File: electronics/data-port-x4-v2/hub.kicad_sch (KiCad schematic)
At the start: 56 parts, among them J1 LEAD, Q1 2N7002, Q2 2N7002, Q3 2N7002, U1 USB2517I-JZX, U2 TCA6408ARGTR, U3 AP2114H-3.3TRG1, U4 H5VU25UC, U5 MAX809S, U6 TCA6408ARGTR, Y1 X322524MSB4SI

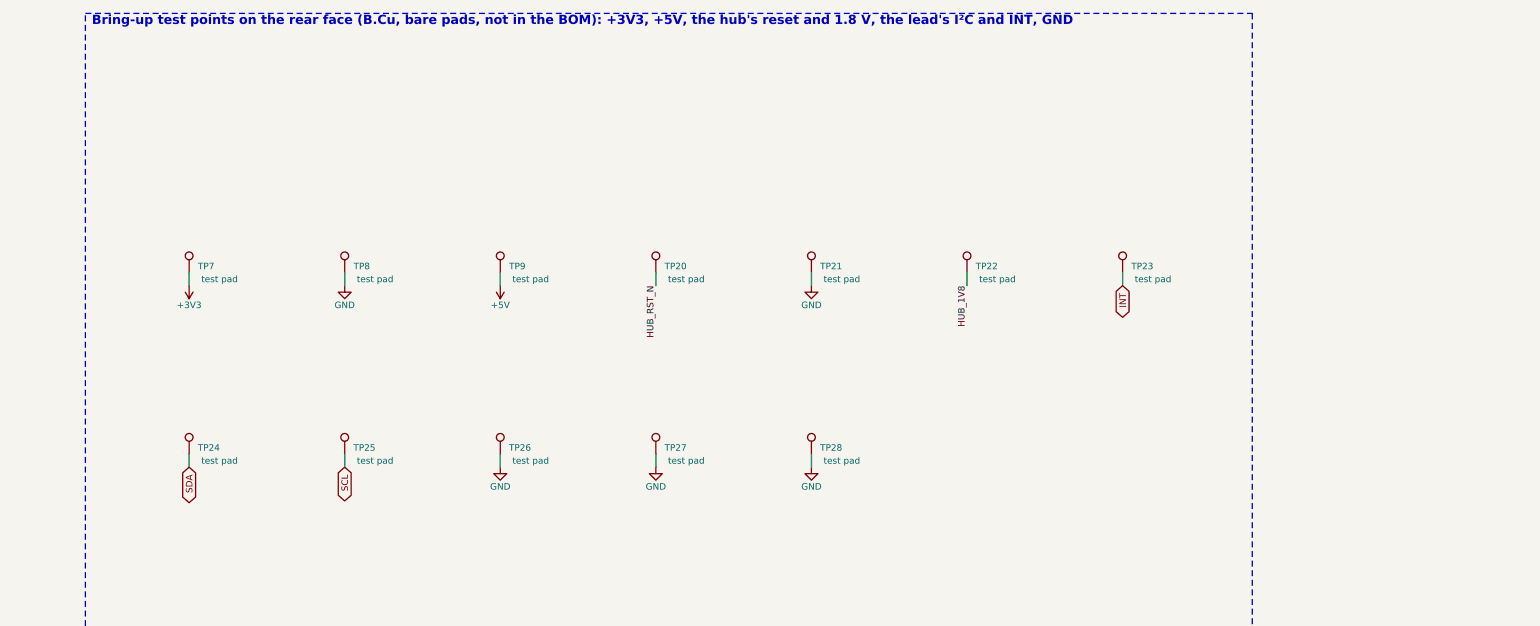
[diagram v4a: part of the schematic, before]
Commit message: DATA x4 v2: rear test pads on buses A-H and the expanders' RESET
Eve's DFT review asked for probe points on the eight crosspoint buses
and on both TCA6408A RESET lines, with a GND beside them.  Eleven bare
rear pads (TPS, out of the BOM and CPL, named on B.SilkS):

- TP29-TP36, buses A to H (1.0 mm), behind the co-processor's east
  side where all eight pass.  A, B, E and F sit on a rear track of their
  own, C, D and G beside one; H, front only, comes down a drawn via.
  Each goes where its bus passes, 2.6 mm or more from the next.
- TP37 GND (1.5 mm), with a drawn via east of it: the automatic one
  went west and moved RN8's +3V3 dog-bones.
- TP38 / TP39 EXP1 / EXP2 RST, each by its pull-up's via.

Every pad is 3.4 mm or more from a THT pad or J1.  The bus group
carries a LOGIC ONLY mark.  The router re-ran only for the new links:
BUS_H's front track moved 0.2 mm onto the new via, and two GND
dog-bones beside it turned.

Co-Authored-By: Claude Opus 5.5 <noreply@anthropic.com>
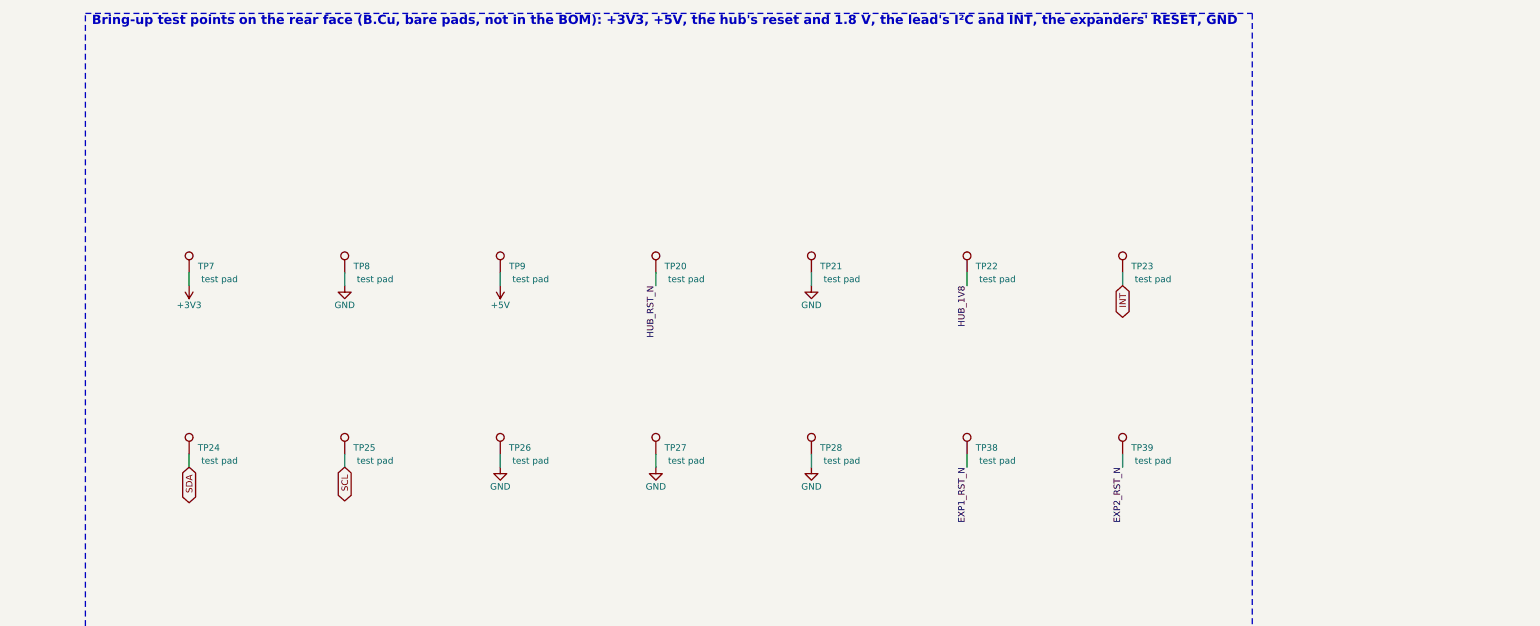
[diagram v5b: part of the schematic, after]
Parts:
- added TP38, TP39: test pad, TestPoint:TestPoint_Pad_D1.0mm, symbol Connector:TestPoint
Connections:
- net EXP1_RST_N: now also TP38.1
- net EXP2_RST_N: now also TP39.1
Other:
- note added: "Bring-up test points on the rear face (B.Cu, bare pads, not in the BOM): +3V3, +5V, the hub's reset and 1.8 V, the lead's I²C and INT, the expanders' RESET, GND"
- note removed: "Bring-up test points on the rear face (B.Cu, bare pads, not in the BOM): +3V3, +5V, the hub's reset and 1.8 V, the lead's I²C and INT, GND"
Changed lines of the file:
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@@
+		)
+	)
+	(symbol
+		(lib_id "Connector:TestPoint")
+		(at 782.32 111.76 0)
+		(unit 1)
+		(exclude_from_sim no)
+		(in_bom no)
+		(on_board yes)
+		(dnp no)
+		(fields_autoplaced yes)
+		(property "Reference" "TP38"
+			(at 786.182 110.49 0)
+			(effects
+				(font
+					(size 1.27 1.27)
+				)
+			)
+		)
+		(property "Value" "test pad"
+			(at 788.282 113.03 0)
+			(effects
+				(font
+					(size 1.27 1.27)
+				)
+			)
+		)
+		(property "Footprint" "TestPoint:TestPoint_Pad_D1.0mm"
+			(at 782.32 111.76 0)
+			(effects
+				(font
+					(size 1.27 1.27)
+				)
+				(hide yes)
+			)
+		)
+		(property "Datasheet" ""
+			(at 782.32 111.76 0)
+			(effects
+				(font
+					(size 1.27 1.27)
+				)
+				(hide yes)
+			)
+		)
+		(property "Description" ""
+			(at 782.32 111.76 0)
+			(effects
+				(font
+					(size 1.27 1.27)
+				)
+				(hide yes)
+			)
+		)
+		(property "MPN" "test pad"
+			(at 782.32 111.76 0)
+			(effects
+				(font
+					(size 1.27 1.27)
+				)
+				(hide yes)
+			)
+		)
+		(property "Manufacturer" "-"
+			(at 782.32 111.76 0)
+			(effects
+				(font
+					(size 1.27 1.27)
+				)
+				(hide yes)
+			)
+		)
+		(pin "1"
+		)
+		(instances
+			(project "data-port-x4-v2"
+				(path "/6eede3c9-04e8-5df8-9dbf-dd766ca3200a/45a04347-8732-5237-9e3b-340287b3f578"
+					(reference "TP38")
+					(unit 1)
+				)
+			)
+		)
+	)
+	(wire
+		(pts
+			(xy 782.32 111.76)
+			(xy 782.32 114.3)
+		)
+		(stroke
+			(width 0)
+			(type default)
+		)
+	)
+	(label "EXP1_RST_N"
+		(at 782.32 114.3 270)
+		(fields_autoplaced yes)
+		(effects
+			(font
+				(size 1.27 1.27)
+			)
+			(justify right bottom)
+		)
+	)
+	(symbol
+		(lib_id "Connector:TestPoint")
+		(at 812.8 111.76 0)
+		(unit 1)
+		(exclude_from_sim no)
+		(in_bom no)
+		(on_board yes)
+		(dnp no)
+		(fields_autoplaced yes)
+		(property "Reference" "TP39"
+			(at 816.662 110.49 0)
+			(effects
+				(font
+					(size 1.27 1.27)
+				)
+			)
+		)
+		(property "Value" "test pad"
+			(at 818.762 113.03 0)
+			(effects
+				(font
+					(size 1.27 1.27)
+				)
+			)
+		)
+		(property "Footprint" "TestPoint:TestPoint_Pad_D1.0mm"
+			(at 812.8 111.76 0)
+			(effects
+				(font
+					(size 1.27 1.27)
+				)
+				(hide yes)
+			)
+		)
+		(property "Datasheet" ""
+			(at 812.8 111.76 0)
+			(effects
+				(font
+					(size 1.27 1.27)
+				)
+				(hide yes)
+			)
+		)
+		(property "Description" ""
+			(at 812.8 111.76 0)
+			(effects
+				(font
+					(size 1.27 1.27)
+				)
+				(hide yes)
+			)
+		)
+		(property "MPN" "test pad"
+			(at 812.8 111.76 0)
+			(effects
+				(font
+					(size 1.27 1.27)
+				)
+				(hide yes)
+			)
+		)
+		(property "Manufacturer" "-"
+			(at 812.8 111.76 0)
+			(effects
+				(font
+					(size 1.27 1.27)
+				)
+				(hide yes)
+			)
+		)
+		(pin "1"
+		)
+		(instances
+			(project "data-port-x4-v2"
+				(path "/6eede3c9-04e8-5df8-9dbf-dd766ca3200a/45a04347-8732-5237-9e3b-340287b3f578"
+					(reference "TP39")
+					(unit 1)
+				)
+			)
+		)
+	)
+	(wire
+		(pts
+			(xy 812.8 111.76)
+			(xy 812.8 114.3)
+		)
+		(stroke
+			(width 0)
+			(type default)
+		)
+	)
+	(label "EXP2_RST_N"
+		(at 812.8 114.3 270)
+		(fields_autoplaced yes)
+		(effects
+			(font
+				(size 1.27 1.27)
+			)
+			(justify right bottom)
 		)
 	)
@@
 		)
 	)
-	(text "Bring-up test points on the rear face (B.Cu, bare pads, not in the BOM): +3V3, +5V, the hub's reset and 1.8 V, the lead's I²C and INT, GND"
+	(text "Bring-up test points on the rear face (B.Cu, bare pads, not in the BOM): +3V3, +5V, the hub's reset and 1.8 V, the lead's I²C and INT, the expanders' RESET, GND"
 		(exclude_from_sim no)
 		(at 610.87 27.94 0)
